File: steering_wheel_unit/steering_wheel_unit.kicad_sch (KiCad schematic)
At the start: 20 parts, among them J1 MAIN_CONNECTOR, J10 MODE2_SOCKET, J11 FUEL_CELL_SOCKET, J12 USB_C_Vertical, J13 Additional goldpins, J14 LCD_SOCKET, J15 JTAG_SOCKET, J16 Additional goldpins from MCU, J3 HALF_GAS_SOCKET, J4 MODE1_SOCKET, J5 FULL_GAS_SOCKET, J6 SPEED_RESET_SOCKET, J7 HORN_SOCKET, J8 SC_CLOSE_SOCKET, J9 SUPPLY_SOCKET

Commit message: organize the preliminary layout
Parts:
- C41, C42: footprint Capacitor_SMD:CP_Elec_8x10.5 -> Capacitor_SMD:C_1206_3216Metric
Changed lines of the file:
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@@
 			)
 		)
-		(property "Footprint" "Capacitor_SMD:CP_Elec_8x10.5"
+		(property "Footprint" "Capacitor_SMD:C_1206_3216Metric"
 			(at 39.0652 95.25 0)
 			(effects
@@
 			)
 		)
-		(property "Footprint" "Capacitor_SMD:CP_Elec_8x10.5"
+		(property "Footprint" "Capacitor_SMD:C_1206_3216Metric"
 			(at 49.2252 95.25 0)
 			(effects

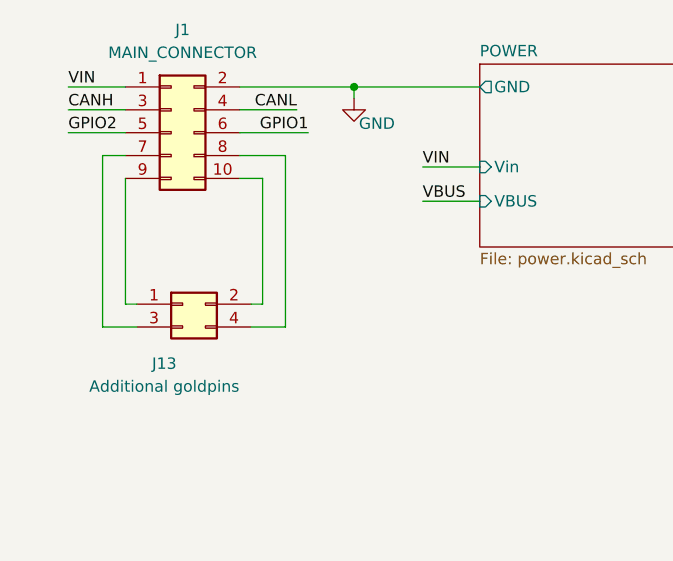
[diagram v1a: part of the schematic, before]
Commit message: Draw part of paths
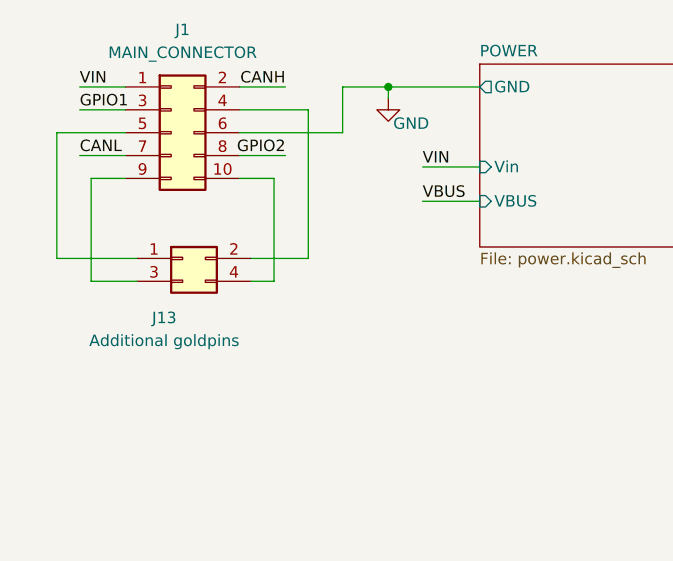
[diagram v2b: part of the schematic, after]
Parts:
- J13: footprint Connector_PinHeader_2.54mm:PinHeader_2x02_P2.54mm_Vertical_SMD -> Connector_PinHeader_2.54mm:PinHeader_2x02_P2.54mm_Vertical
- J16: footprint Connector_PinHeader_1.00mm:PinHeader_1x03_P1.00mm_Vertical_SMD_Pin1Right -> Connector_PinHeader_2.54mm:PinHeader_1x03_P2.54mm_Vertical
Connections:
- net CANH: now also J1.2 (Pin_2); no longer J1.3 (Pin_3)
- net CANL: now also J1.7 (Pin_7); no longer J1.4 (Pin_4)
- net GND: now also J1.6 (Pin_6); no longer J1.2 (Pin_2)
- net GPIO1: now also J1.3 (Pin_3); no longer J1.6 (Pin_6)
- net GPIO2: now also J1.8 (Pin_8); no longer J1.5 (Pin_5)
- net at J13.1 (Pin_1): now also J1.5 (Pin_5); no longer J1.9 (Pin_9)
- net at J13.2 (Pin_2): now also J1.4 (Pin_4); no longer J1.10 (Pin_10)
- net at J13.3 (Pin_3): now also J1.9 (Pin_9); no longer J1.7 (Pin_7)
- net at J13.4 (Pin_4): now also J1.10 (Pin_10); no longer J1.8 (Pin_8)
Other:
- moved on the sheet: J13

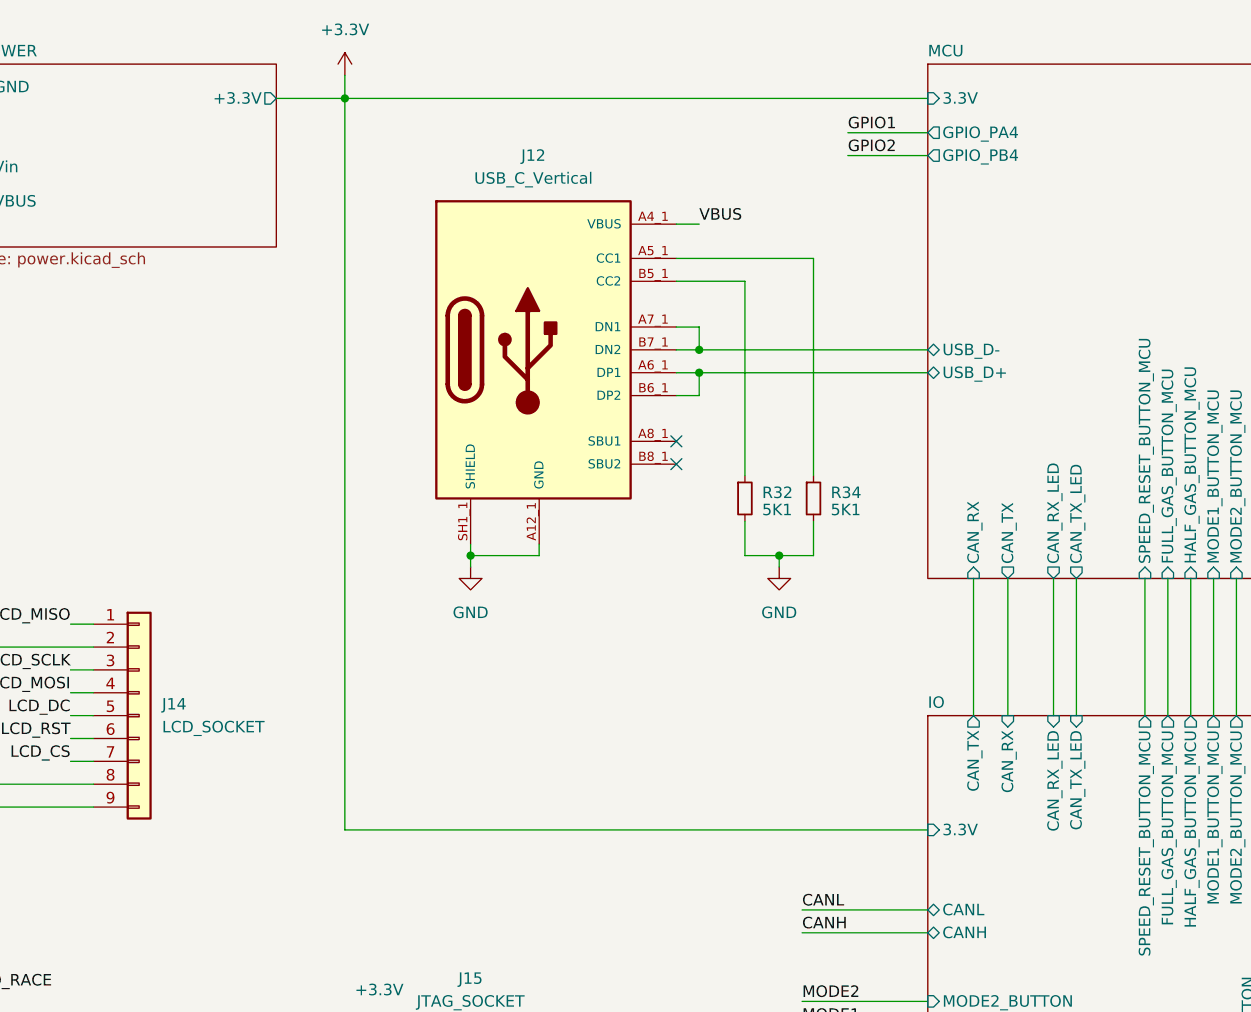
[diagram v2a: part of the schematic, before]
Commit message: Add zones for gnd and power
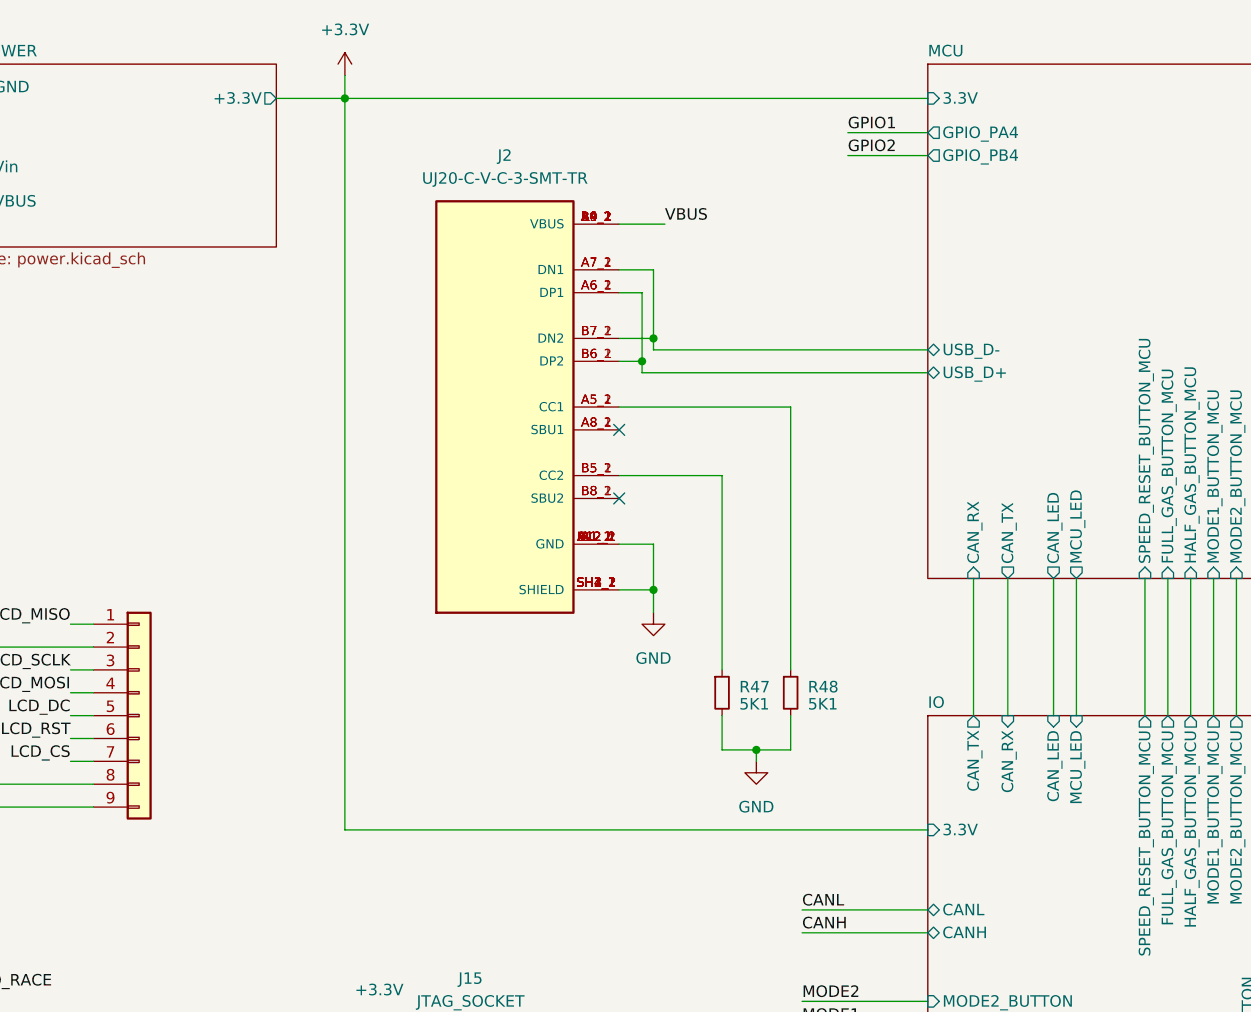
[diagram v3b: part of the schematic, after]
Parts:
- removed J12: USB_C_Vertical, Lib:CUI_UJ20-C-V-C-3-SMT-TR, symbol UJ20-C-V-C-3-SMT-TR:UJ20-C-V-C-3-SMT-TR
- removed R32, R34: 5K1, Resistor_SMD:R_1206_3216Metric, symbol Device:R_Small
- added J2: UJ20-C-V-C-3-SMT-TR, Lib:CUI_UJ20-C-V-C-2-SMT-TR, symbol UJ20-C-V-C-3-SMT-TR:UJ20-C-V-C-3-SMT-TR
- added R47, R48: 5K1, Resistor_SMD:R_1206_3216Metric, symbol Device:R_Small
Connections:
- net GND: now also J2.A12_1 (GND), J2.A12_2 (GND), J2.A1_1 (GND), J2.A1_2 (GND), J2.B12_1 (GND), J2.B12_2 (GND), J2.B1_1 (GND), J2.B1_2 (GND), J2.SH1_1 (SHIELD), J2.SH1_2 (SHIELD), J2.SH2_1 (SHIELD), J2.SH2_2 (SHIELD), J2.SH3_1 (SHIELD), J2.SH3_2 (SHIELD), J2.SH4_1 (SHIELD), J2.SH4_2 (SHIELD), R47.2, R48.2
- net MCU/USB_D+: now also J2.A6_1 (DP1), J2.A6_2 (DP1), J2.B6_1 (DP2), J2.B6_2 (DP2)
- net MCU/USB_D-: now also J2.A7_1 (DN1), J2.A7_2 (DN1), J2.B7_1 (DN2), J2.B7_2 (DN2)
- net VBUS: now also J2.A4_1 (VBUS), J2.A4_2 (VBUS), J2.A9_1 (VBUS), J2.A9_2 (VBUS), J2.B4_1 (VBUS), J2.B4_2 (VBUS), J2.B9_1 (VBUS), J2.B9_2 (VBUS)
- new net: J2.B5_1 (CC2), J2.B5_2 (CC2), R47.1
- new net: J2.A5_1 (CC1), J2.A5_2 (CC1), R48.1
- new net: J2.A8_1 (SBU1), J2.A8_2 (SBU1)
- new net: J2.B8_1 (SBU2), J2.B8_2 (SBU2)
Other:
- sheet IO ports: added CAN_LED, MCU_LED; removed CAN_RX_LED, CAN_TX_LED
- sheet MCU ports: added CAN_LED, MCU_LED; removed CAN_RX_LED, CAN_TX_LED

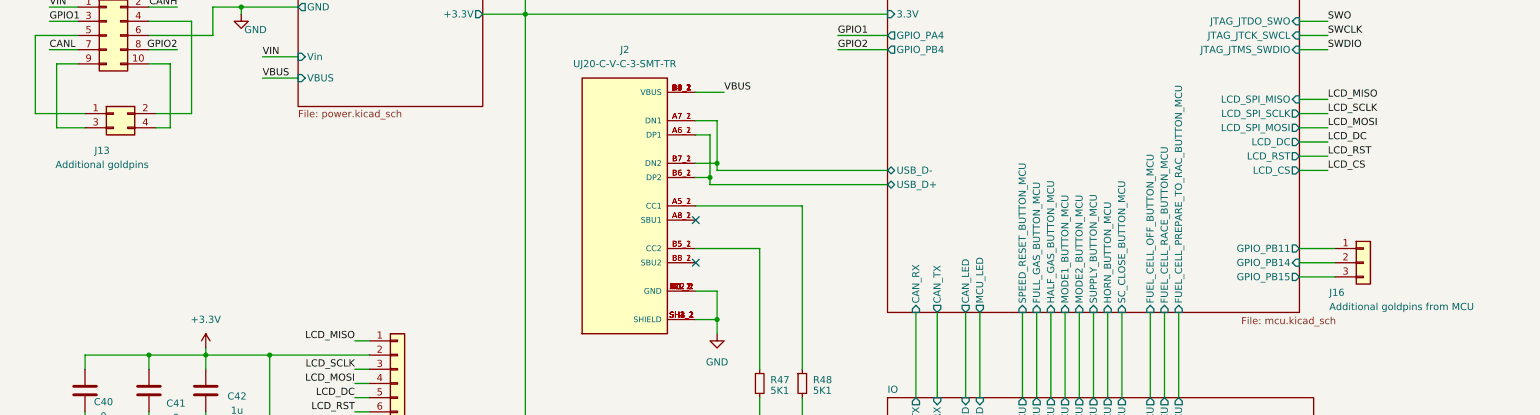
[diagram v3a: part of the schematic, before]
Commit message: Edit tracks and add captions of elements
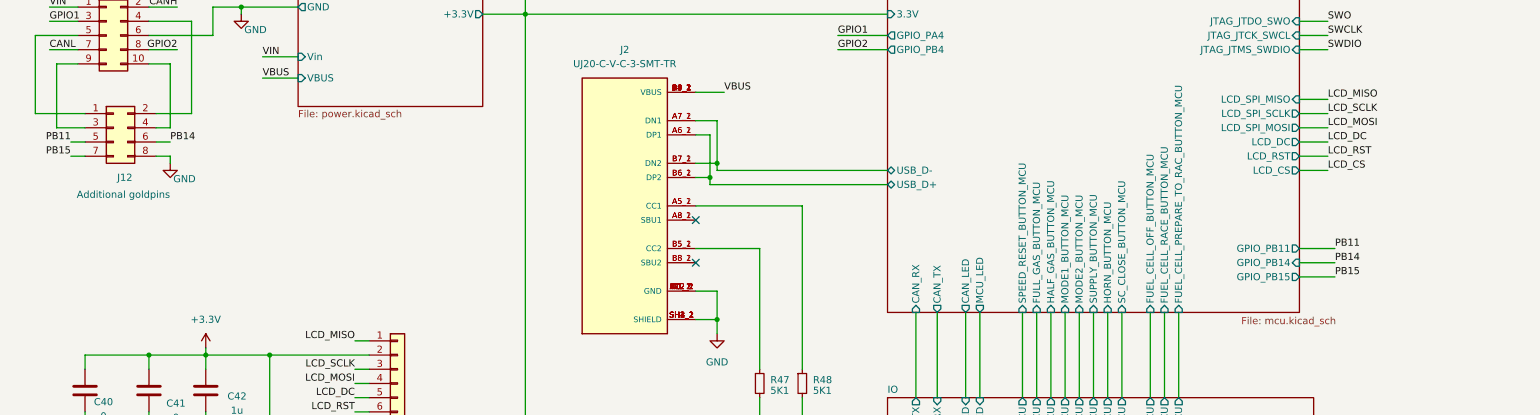
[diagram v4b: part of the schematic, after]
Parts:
- removed J13: Additional goldpins, Connector_PinHeader_2.54mm:PinHeader_2x02_P2.54mm_Vertical, symbol Connector_Generic:Conn_02x02_Odd_Even
- removed J16: Additional goldpins from MCU, Connector_PinHeader_2.54mm:PinHeader_1x03_P2.54mm_Vertical, symbol Connector_Generic:Conn_01x03
- added J12: Additional goldpins, Connector_PinHeader_2.54mm:PinHeader_2x04_P2.54mm_Vertical, symbol Connector_Generic:Conn_02x04_Odd_Even
- J2: footprint Lib:CUI_UJ20-C-V-C-2-SMT-TR -> Lib:CUI_UJ20-C-V-C-3-SMT-TR
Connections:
- net GND: now also J12.8 (Pin_8)
- net at J1.5 (Pin_5): now also J12.1 (Pin_1)
- net at J1.4 (Pin_4): now also J12.2 (Pin_2)
- net at J1.9 (Pin_9): now also J12.3 (Pin_3)
- net at J1.10 (Pin_10): now also J12.4 (Pin_4)
- new net PB11: J12.5 (Pin_5)
- new net PB14: J12.6 (Pin_6)
- new net PB15: J12.7 (Pin_7)

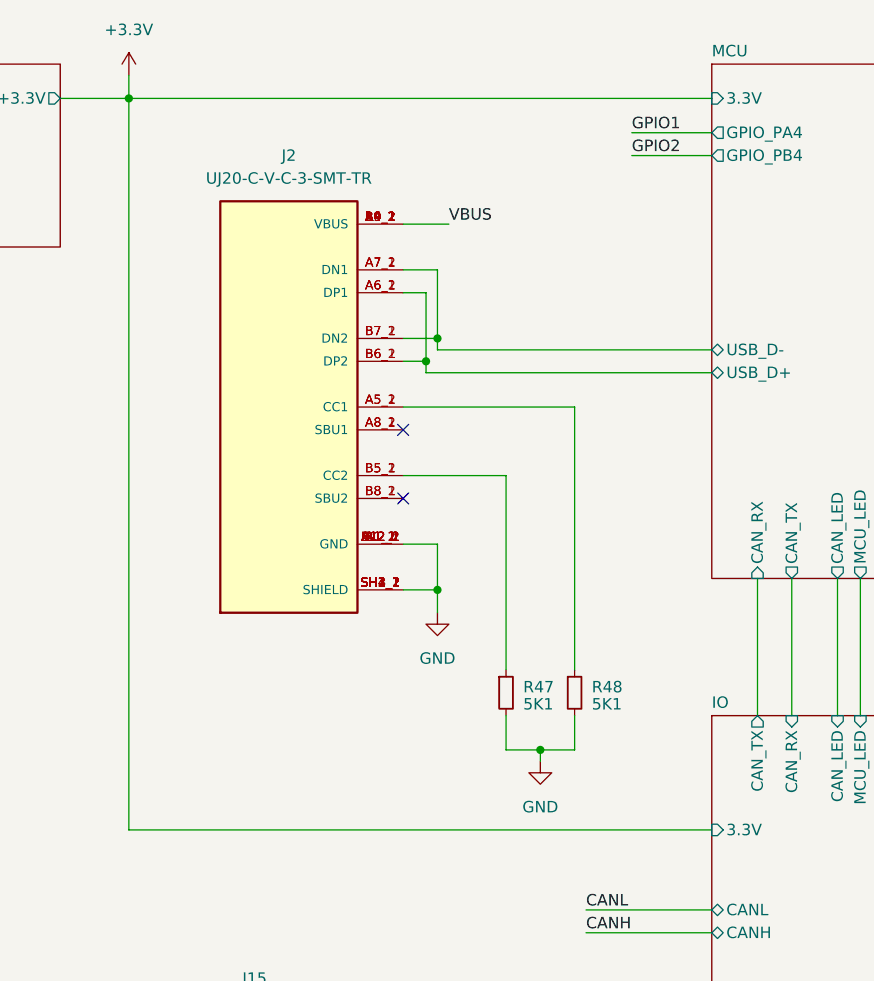
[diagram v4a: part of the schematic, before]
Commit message: Add dimensions
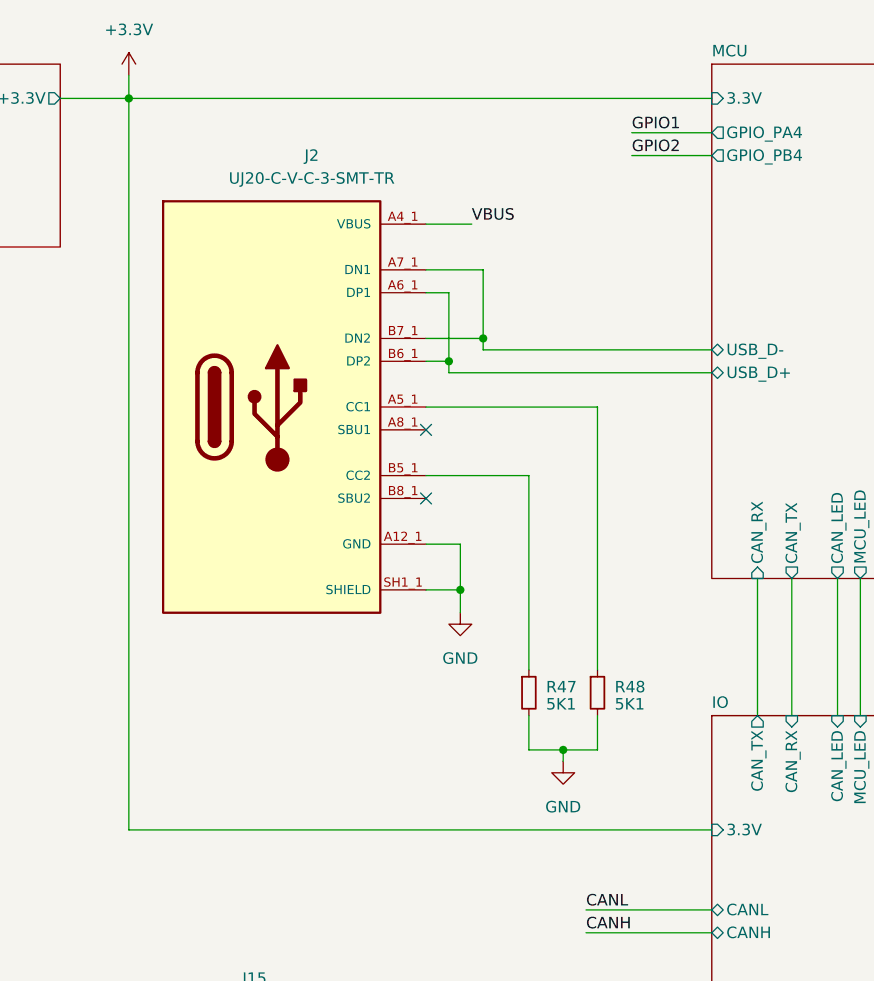
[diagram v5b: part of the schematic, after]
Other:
- title: (none) -> Steering_wheel_unit_main
- moved on the sheet: R47, R48

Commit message: Add manufacturing
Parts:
- renumbered J14 to J13, J15 to J14
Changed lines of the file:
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@@
 		(dnp no)
 		(fields_autoplaced yes)
-		(property "Reference" "J14"
+		(property "Reference" "J13"
 			(at 85.09 91.4399 0)
 			(effects
@@
 				)
 				(justify left)
-				(hide yes)
 			)
 		)
@@
 				)
 				(justify left)
-				(hide yes)
 			)
 		)
@@
 			(project "steering_wheel_unit"
 				(path "/b435671d-bfd7-4707-b36e-3eecb7fa1f89"
-					(reference "J14")
+					(reference "J13")
 					(unit 1)
 				)
@@
 		(dnp no)
 		(fields_autoplaced yes)
-		(property "Reference" "J15"
+		(property "Reference" "J14"
 			(at 119.38 121.92 0)
 			(effects
@@
 			(project "steering_wheel_unit"
 				(path "/b435671d-bfd7-4707-b36e-3eecb7fa1f89"
-					(reference "J15")
+					(reference "J14")
 					(unit 1)
 				)
